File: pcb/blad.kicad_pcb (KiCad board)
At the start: 2 copper layers, 228.6 x 76.2 mm, 93 parts, among them J1 Conn_01x04, J2 Conn_01x02_Pin, SW1 1U, SW10 1U, SW11 1U, SW12 1U, SW13 1.25U, SW14 1U, SW15 1U, SW16 1U, SW17 1U, SW18 1U, SW19 1U, SW2 1U, SW20 1U, SW21 1U, SW22 1U, SW23 1.75U, SW24 1U, SW25 1U, SW26 1U, SW27 1U, SW28 1U, SW29 1U, SW3 1U, SW30 1U, SW31 1U, SW32 1U, SW33 1.25U, SW34 1.25U, SW35 1U, SW36 1.25U, SW37 2.75U, SW38 1.25U, SW39 1U, SW4 1U, SW40 1.25U, SW41 1.75U, SW42 2.25U, SW5 1U, SW6 1U, SW7 1U, SW8 1U, SW9 1U, U1 HY0020

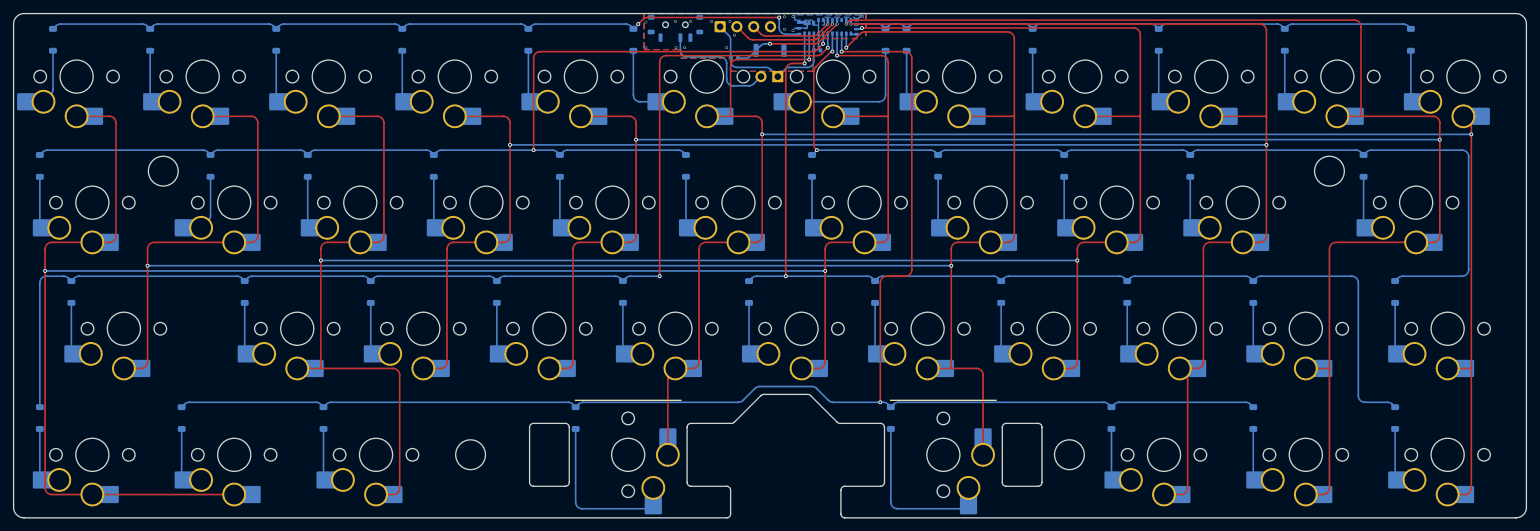
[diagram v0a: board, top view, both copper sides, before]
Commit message: Update PCB design for ANNA-B402
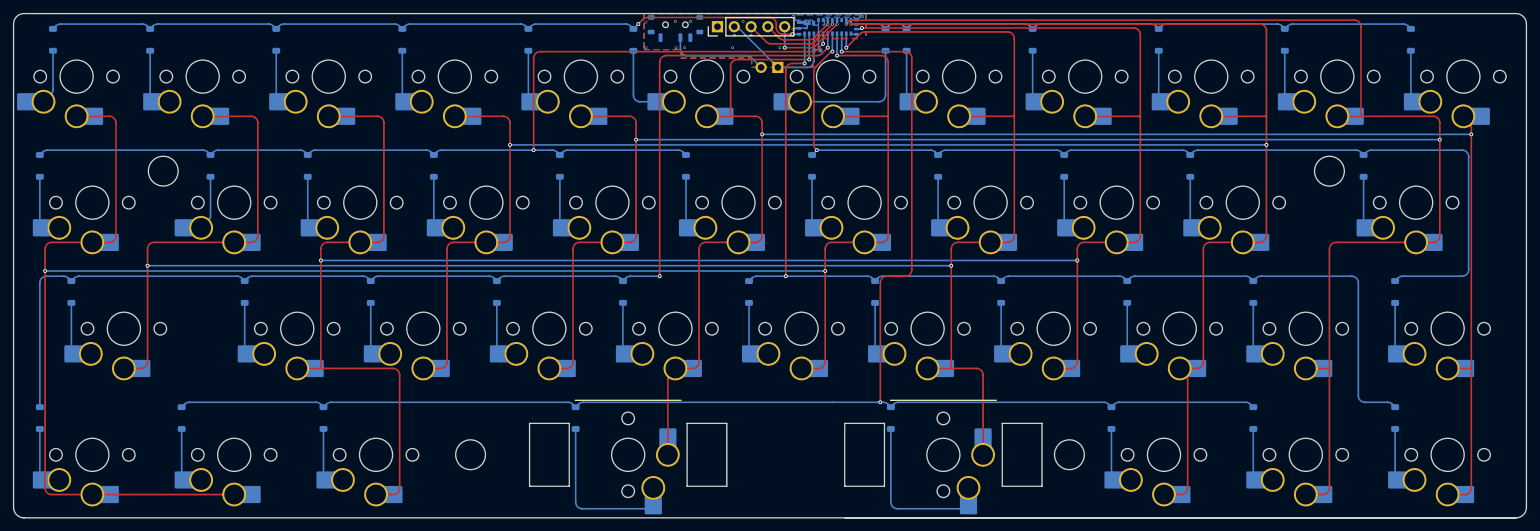
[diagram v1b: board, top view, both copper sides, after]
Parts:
- removed J1: Conn_01x04, Connector_PinHeader_2.54mm:PinHeader_1x04_P2.54mm_Vertical
- removed R1: 10k, Resistor_SMD:R_0402_1005Metric
- removed TS1: RST, Button_Switch_SMD:SW_Push_SPST_NO_Alps_SKRK
- added J3: Conn_01x05, Connector_PinHeader_2.54mm:PinHeader_1x05_P2.54mm_Vertical, F.Cu at (196.1, 111.5)
- moved J2 1.39 mm to (205.2, 117.7)
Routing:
- net +3V0: track 24.6 -> 19.2 mm
- net nRESET: track 17.6 -> 13.1 mm
- net Net-(J2-Pin_2): track 18.6 -> 15.1 mm
- net SWDIO: track 17.6 -> 15.1 mm
- net ROW6: track 235.9 -> 234.1 mm
- net SWDCLK: track 13.0 -> 11.4 mm
- net GND: vias 15 -> 14
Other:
- outline, holes or cut-outs redrawn
